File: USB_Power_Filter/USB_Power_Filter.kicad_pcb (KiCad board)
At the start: 2 copper layers, 30 x 12 mm, 7 parts

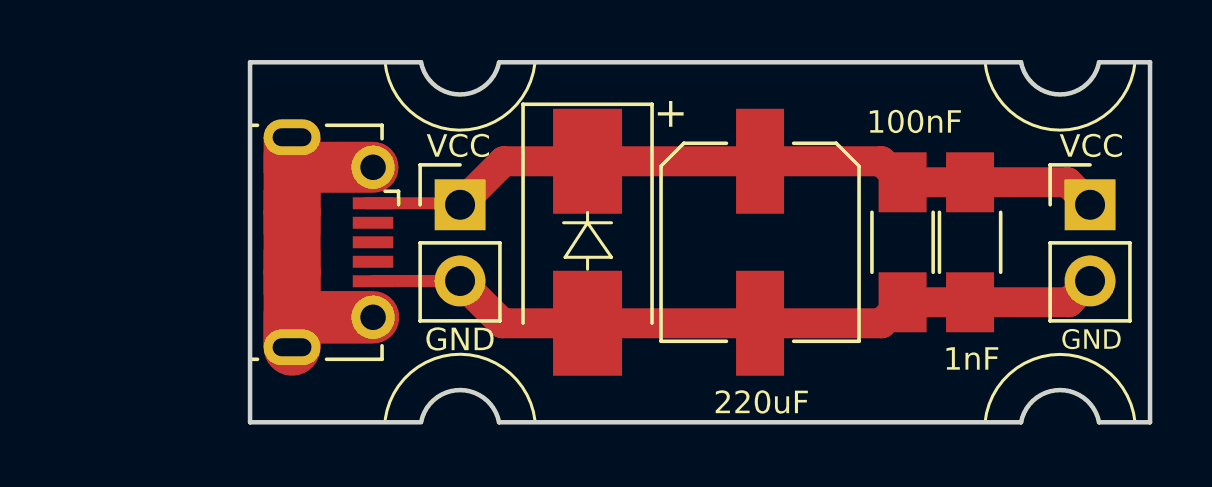
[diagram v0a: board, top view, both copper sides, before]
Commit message: Adding NEMA0183
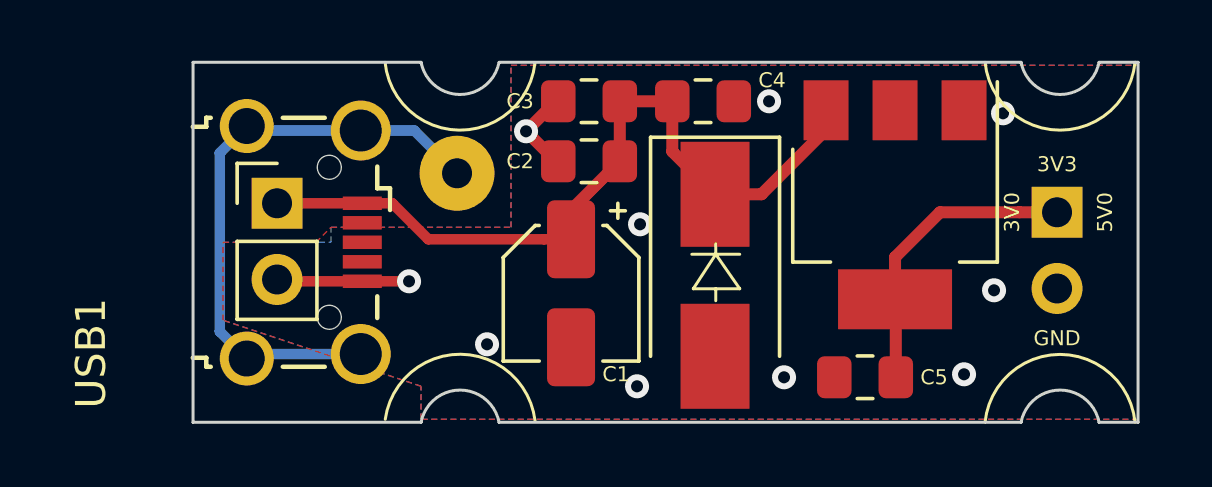
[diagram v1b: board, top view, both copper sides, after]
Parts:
- added C4: 1nF, Capacitor_SMD:C_0805_2012Metric_Pad1.15x1.40mm_HandSolder, F.Cu at (138.1, 115.3)
- added C5: 4.7uF, Capacitor_SMD:C_0805_2012Metric_Pad1.15x1.40mm_HandSolder, F.Cu at (143.5, 124.5)
- added U1: LDL1117S, Package_TO_SOT_SMD:SOT-223-3_TabPin2, F.Cu at (144.5, 118.8)
- added USB SHIELD: Conn_01x01_Female, Connector_Wire:SolderWirePad_1x01_Drill1mm, B.Cu at (129.9, 117.7)
- C1: value 220uF -> UCL1E100MCL; footprint Capacitors_SMD:CP_Elec_6.3x5.8 -> Capacitor_SMD:CP_Elec_4x5.8
- C2: value 100nF -> 1uF; footprint Capacitors_SMD:C_1206_HandSoldering -> Capacitor_SMD:C_0805_2012Metric_Pad1.15x1.40mm_HandSolder
- C3: value 1nF -> 100nF; footprint Capacitors_SMD:C_1206_HandSoldering -> Capacitor_SMD:C_0805_2012Metric_Pad1.15x1.40mm_HandSolder
- D1: footprint Diodes_SMD:D_SMB_Handsoldering -> Diode_SMD:D_SMB_Handsoldering
- POWER1: footprint Pin_Headers:Pin_Header_Straight_1x02_Pitch2.54mm -> Connector_PinHeader_2.54mm:PinHeader_1x02_P2.54mm_Vertical; moved to B.Cu
- POWER_IN1: footprint Pin_Headers:Pin_Header_Straight_1x02_Pitch2.54mm -> Connector_PinHeader_2.54mm:PinHeader_1x02_P2.54mm_Vertical
- USB1: value USB_B_Micro -> Wuerth_629105150521; footprint Connectors_USB:USB_Micro-B_Molex-105017-0001 -> Connector_USB:USB_Micro-B_Wuerth_629105150521_CircularHoles
- moved C3 13.5 mm to (134.3, 115.3), turned to 180 degrees
- moved C2 10.8 mm to (134.3, 117.3), turned to 180 degrees
- moved C1 6.53 mm to (133.7, 121.7)
- moved POWER_IN1 6.10 mm to (123.9, 118.7)
- moved D1 4.39 mm to (138.5, 121.1)
- moved POWER1 1.13 mm to (149.9, 119.0), turned to 180 degrees
- moved USB1 0.09 mm to (124.8, 120.0)
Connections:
- C1 pad 2: Net-(C1-Pad2) -> GND
- C2 pad 2: Net-(C1-Pad2) -> GND
- C3 pad 2: Net-(C1-Pad2) -> GND
- D1 pad 2: Net-(C1-Pad2) -> GND
- POWER1 pad 1: Net-(C1-Pad1) -> Net-(C5-Pad1)
- POWER1 pad 2: Net-(C1-Pad2) -> GND
- POWER_IN1 pad 2: Net-(C1-Pad2) -> GND
- USB1 pad 2: Net-(DATA1-Pad1) -> (no net)
- USB1 pad 3: Net-(DATA1-Pad2) -> (no net)
- USB1 pad 4: Net-(DATA1-Pad3) -> (no net)
- USB1 pad 5: Net-(C1-Pad2) -> GND
- USB1 pad 6: Net-(C1-Pad2) -> Net-(SHIELD1-Pad1)
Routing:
- net Net-(C1-Pad2): track 36.3 -> 0.00 mm
- net Net-(SHIELD1-Pad1): track 0.00 -> 20.0 mm
- net Net-(C5-Pad1): track 0.00 -> 10.0 mm
- net GND: track 0.00 -> 7.40 mm, vias 0 -> 10
- net Net-(C1-Pad1): track 25.6 -> 26.3 mm
- added copper zone on B.Cu, net GND
- added copper zone on F.Cu, net GND
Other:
- board size 30 x 12 mm -> 31.5 x 12 mm
- net class Default: trace_width 0.25 -> 0.35
- board text added: "3V0"
- board text added: "3V3"
- board text added: "5V0"
- board text removed: "VCC"

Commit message: More PCB work on USB power filter
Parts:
- moved POWER1 0.32 mm to (150.0, 118.7)
- moved POWER_IN1 0.08 mm to (123.8, 118.7)
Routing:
- net GND: track 7.40 -> 0.15 mm, vias 10 -> 13
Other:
- net class Default: trace_width 0.35 -> 0.45
- rule pad_to_mask_clearance: 0.2 -> 0.0508
- board text added: "Mount 20.0mm x 12.5mm OC M2.5"

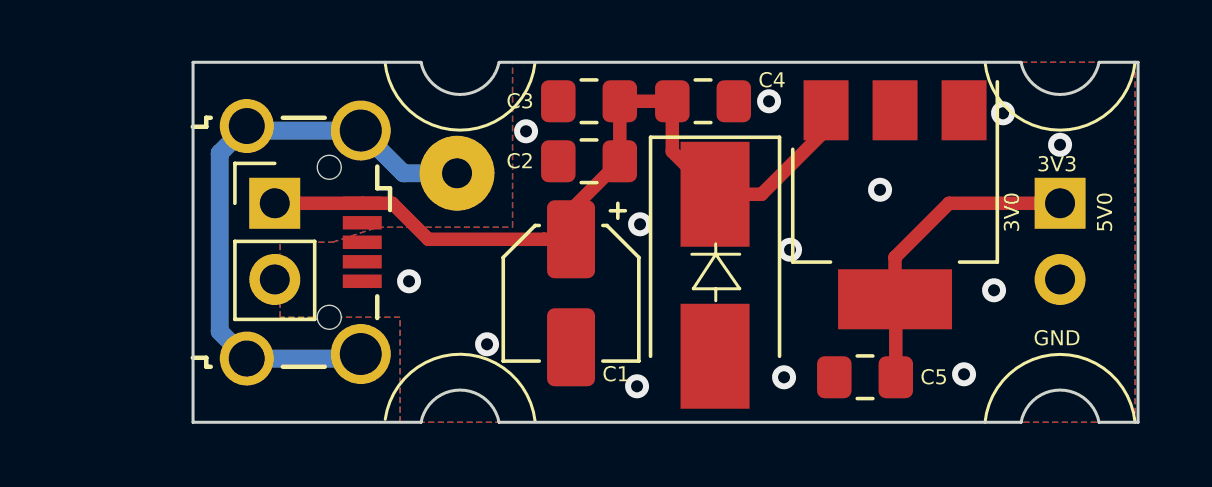
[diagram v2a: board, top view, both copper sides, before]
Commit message: Two alternatives for the USB power filter
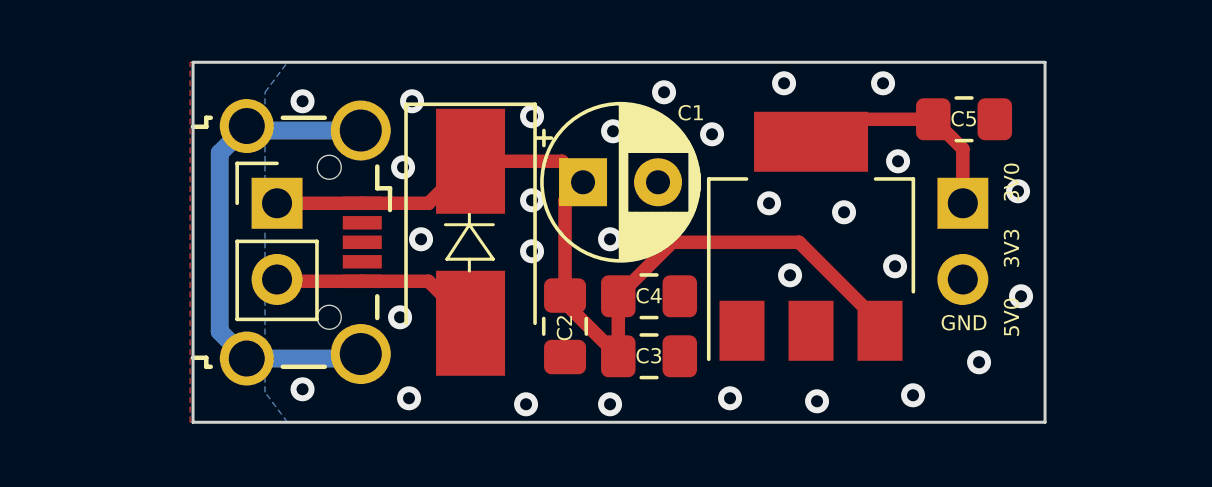
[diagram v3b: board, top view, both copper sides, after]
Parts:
- removed USB SHIELD: Conn_01x01_Female, Connector_Wire:SolderWirePad_1x01_Drill1mm
- C1: value UCL1E100MCL -> 100u; footprint Capacitor_SMD:CP_Elec_4x5.8 -> Capacitor_THT:CP_Radial_D5.0mm_P2.50mm
- moved C5 9.21 mm to (146.8, 115.9), turned to 0 degrees
- moved C3 8.73 mm to (136.3, 123.8), turned to 0 degrees
- moved D1 8.22 mm to (130.3, 120.0)
- moved C4 6.74 mm to (136.3, 121.8)
- moved C2 5.56 mm to (133.5, 122.8), turned to 270 degrees
- moved C1 3.72 mm to (134.1, 118.0), turned to 0 degrees
- moved POWER1 3.24 mm to (146.8, 118.7)
- moved U1 2.99 mm to (141.7, 119.8), turned to 90 degrees
- moved POWER_IN1 0.08 mm to (123.9, 118.7)
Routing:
- net GND: track 0.15 -> 7.05 mm, vias 13 -> 29
- net Net-(C1-Pad1): track 26.3 -> 30.7 mm
- net Net-(SHIELD1-Pad1): track 20.2 -> 16.2 mm
- net Net-(C5-Pad1): track 10.3 -> 7.59 mm
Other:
- board size 31.5 x 12 mm -> 28.4 x 12 mm
- board text removed: "Mount 20.0mm x 12.5mm OC M2.5"

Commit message: As sent to fab
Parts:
- D1: footprint Diode_SMD:D_SMB_Handsoldering -> Diode_SMD:D_SOD-323_HandSoldering
- moved C5 14.3 mm to (135.6, 124.8), turned to 180 degrees
- moved C3 8.59 mm to (134.5, 115.4), turned to 180 degrees
- moved C4 6.68 mm to (138.2, 115.4)
- moved C2 5.76 mm to (131.8, 117.3), turned to 180 degrees
- moved C1 2.22 mm to (132.8, 119.8), turned to 270 degrees
- moved U1 2.21 mm to (139.9, 121.2), turned to 270 degrees
- moved D1 1.25 mm to (129.1, 120.0)
- moved POWER1 0.90 mm to (145.9, 118.3)
- moved POWER_IN1 0.40 mm to (124.0, 118.3)
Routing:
- net Net-(C1-Pad1): track 30.7 -> 19.9 mm
- net Net-(C5-Pad1): track 7.59 -> 12.0 mm
- net GND: track 7.05 -> 5.32 mm, vias 29 -> 28
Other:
- board size 28.4 x 12 mm -> 27.7 x 12 mm
- board text added: "Mount 16.0mm x 12.5mm OC M2.5"

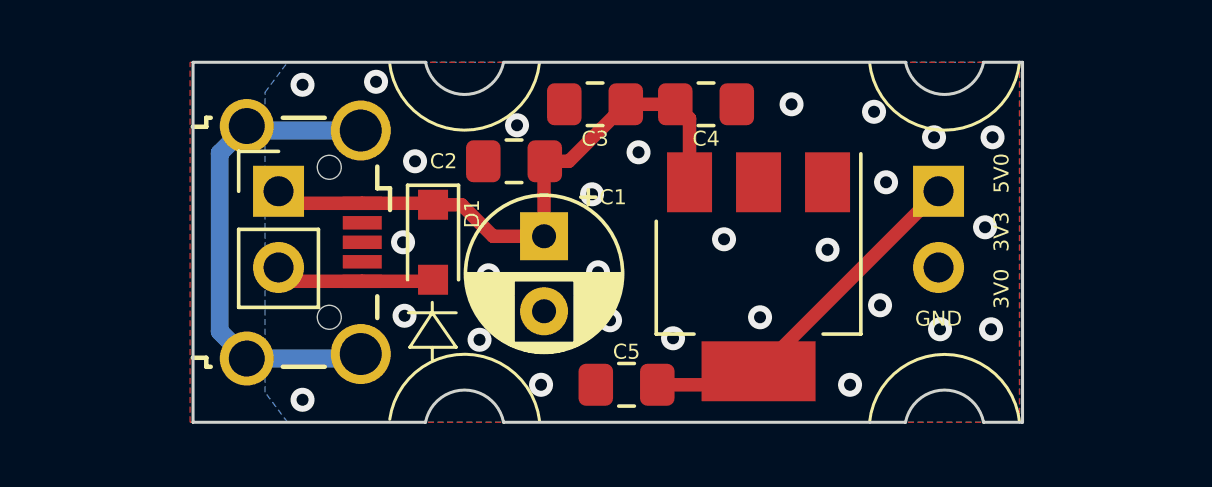
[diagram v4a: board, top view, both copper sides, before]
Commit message: Slight mods to USB power filter
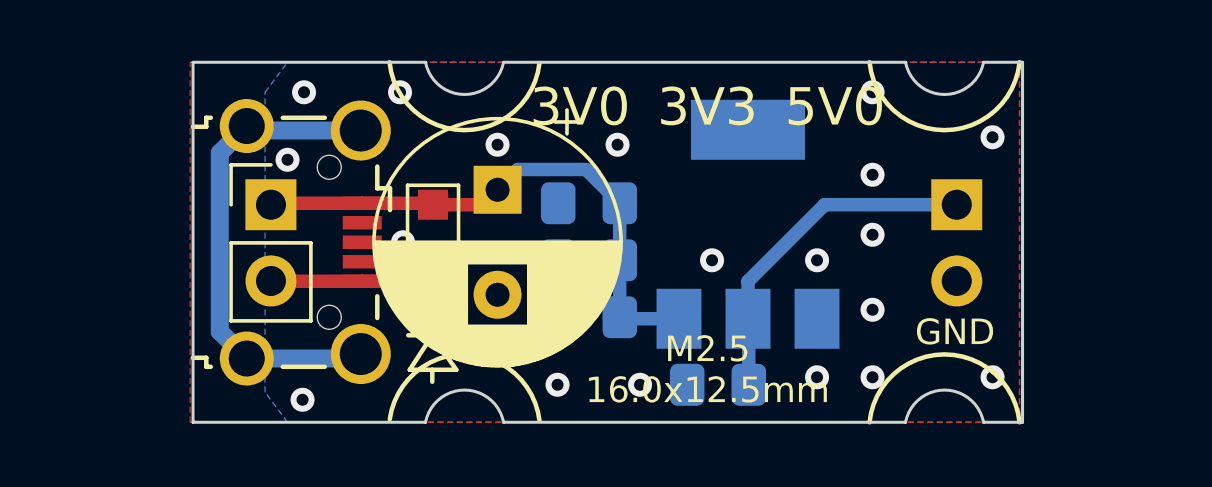
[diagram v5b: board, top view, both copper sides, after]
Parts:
- C1: footprint Capacitor_THT:CP_Radial_D5.0mm_P2.50mm -> Capacitor_THT:CP_Radial_D8.0mm_P3.50mm
- C2, C3, C4, C5, U1: moved to B.Cu
- moved C4 8.10 mm to (134.3, 122.5), turned to 180 degrees
- moved C3 5.20 mm to (134.3, 120.6)
- moved C5 3.05 mm to (138.6, 124.8)
- moved C2 2.87 mm to (134.3, 118.7)
- moved C1 2.19 mm to (131.2, 118.2)
- moved U1 1.78 mm to (139.6, 119.4), turned to 90 degrees
- moved POWER1 0.76 mm to (146.6, 118.8)
- moved POWER_IN1 0.52 mm to (123.7, 118.8)
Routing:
- net Net-(C1-Pad1): track 19.9 -> 18.5 mm
- net Net-(C5-Pad1): track 12.0 -> 11.5 mm
- net GND: track 5.32 -> 5.43 mm, vias 28 -> 19
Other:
- board text added: "M2.5 16.0x12.5mm"
- board text removed: "Mount 16.0mm x 12.5mm OC M2.5"
